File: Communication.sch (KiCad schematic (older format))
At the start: 24 parts, among them IC1 LAN8720

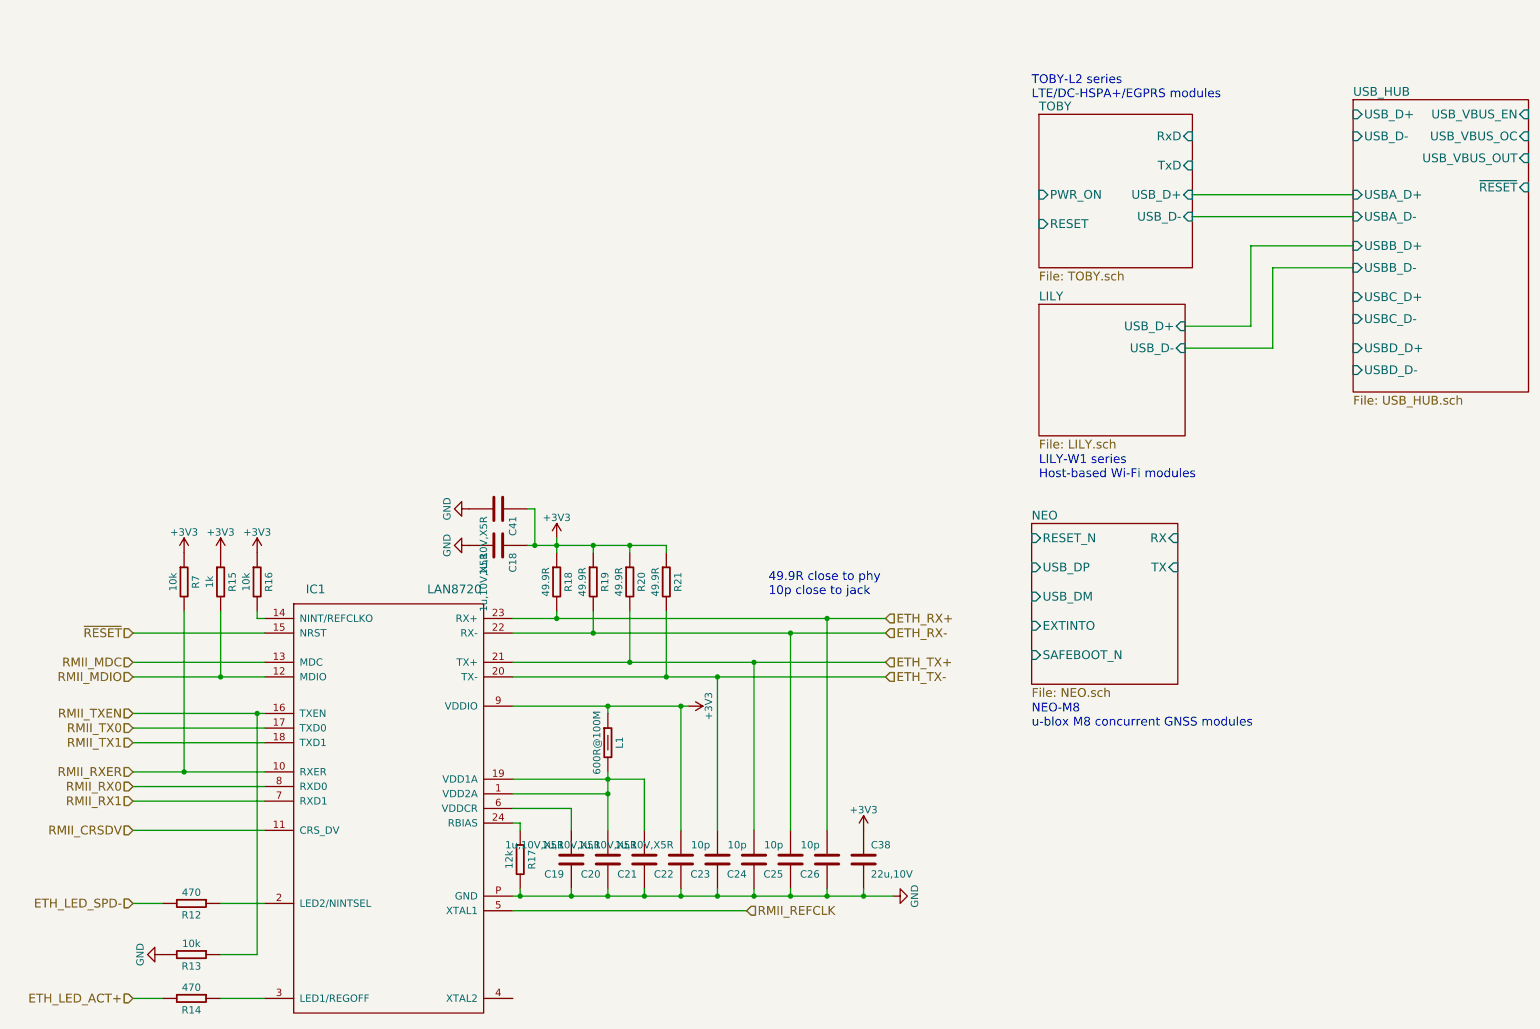
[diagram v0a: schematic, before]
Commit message: LAN Transformer footprint ergänzt
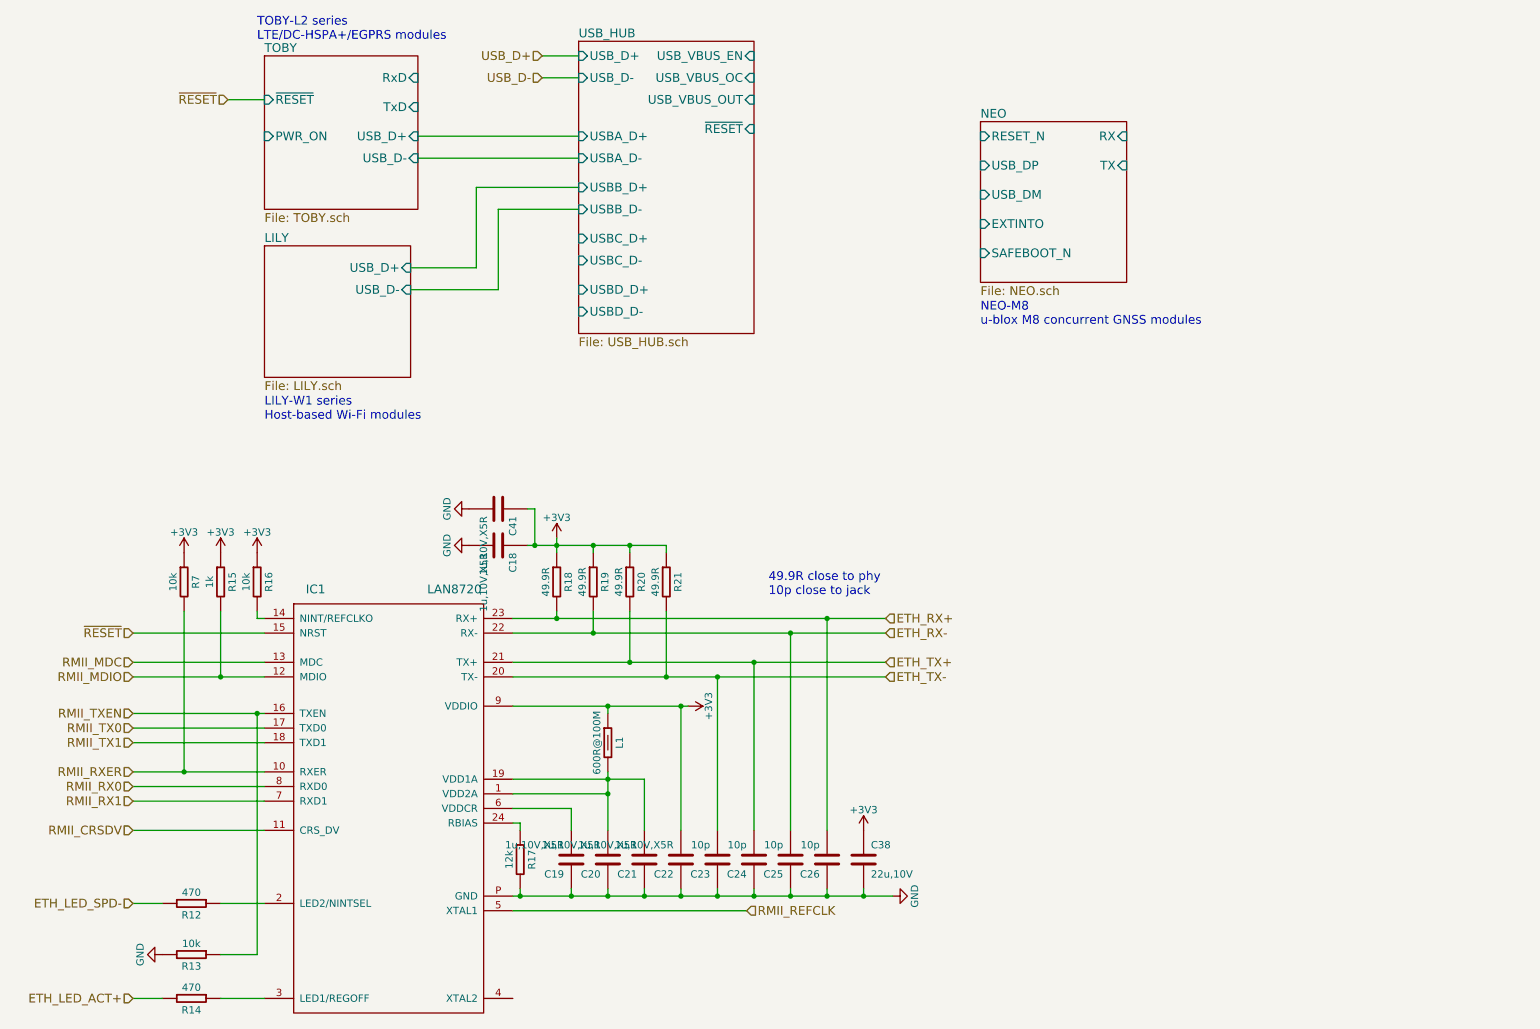
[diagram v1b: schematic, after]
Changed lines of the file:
@@
 	1400 6300 2300 6300
 $Sheet
-S 7600 1400 1050 1050
+S 2300 1000 1050 1050
 U 570DCCC5
 F0 "TOBY" 60
 F1 "TOBY.sch" 60
-F2 "PWR_ON" I L 7600 1950 60
-F3 "RESET" I L 7600 2150 60
-F4 "RxD" I R 8650 1550 60
-F5 "TxD" I R 8650 1750 60
-F6 "USB_D+" I R 8650 1950 60
-F7 "USB_D-" I R 8650 2100 60
+F2 "PWR_ON" I L 2300 1550 60
+F3 "RxD" I R 3350 1150 60
+F4 "TxD" I R 3350 1350 60
+F5 "USB_D+" I R 3350 1550 60
+F6 "USB_D-" I R 3350 1700 60
+F7 "~RESET" I L 2300 1300 60
 $EndSheet
-Text Notes 7550 1300 0    60   ~ 0
+Text Notes 2250 900  0    60   ~ 0
 TOBY-L2 series \nLTE/DC-HSPA+/EGPRS modules \n
 $Sheet
-S 7600 2700 1000 900
+S 2300 2300 1000 900
 U 57112592
 F0 "LILY" 60
 F1 "LILY.sch" 60
-F2 "USB_D+" I R 8600 2850 60
-F3 "USB_D-" I R 8600 3000 60
+F2 "USB_D+" I R 3300 2450 60
+F3 "USB_D-" I R 3300 2600 60
 $EndSheet
 $Sheet
-S 7550 4200 1000 1100
+S 7200 1450 1000 1100
 U 5712437A
 F0 "NEO" 60
 F1 "NEO.sch" 60
-F2 "RESET_N" I L 7550 4300 60
-F3 "USB_DP" I L 7550 4500 60
-F4 "USB_DM" I L 7550 4700 60
-F5 "EXTINTO" I L 7550 4900 60
-F6 "SAFEBOOT_N" I L 7550 5100 60
-F7 "RX" I R 8550 4300 60
-F8 "TX" I R 8550 4500 60
+F2 "RESET_N" I L 7200 1550 60
+F3 "USB_DP" I L 7200 1750 60
+F4 "USB_DM" I L 7200 1950 60
+F5 "EXTINTO" I L 7200 2150 60
+F6 "SAFEBOOT_N" I L 7200 2350 60
+F7 "RX" I R 8200 1550 60
+F8 "TX" I R 8200 1750 60
 $EndSheet
-Text Notes 7600 3900 0    60   ~ 0
+Text Notes 2300 3500 0    60   ~ 0
 LILY-W1 series \nHost-based Wi-Fi modules
-Text Notes 7550 5600 0    60   ~ 0
+Text Notes 7200 2850 0    60   ~ 0
 NEO-M8 \nu-blox M8 concurrent GNSS modules
 $Sheet
-S 9750 1300 1200 2000
+S 4450 900  1200 2000
 U 571531BA
 F0 "USB_HUB" 60
 F1 "USB_HUB.sch" 60
-F2 "USB_D+" I L 9750 1400 60
-F3 "USB_D-" I L 9750 1550 60
-F4 "USBA_D+" I L 9750 1950 60
-F5 "USBA_D-" I L 9750 2100 60
-F6 "USBB_D+" I L 9750 2300 60
-F7 "USBB_D-" I L 9750 2450 60
-F8 "USBC_D+" I L 9750 2650 60
-F9 "USBC_D-" I L 9750 2800 60
-F10 "USBD_D+" I L 9750 3000 60
-F11 "USBD_D-" I L 9750 3150 60
-F12 "~RESET" I R 10950 1900 60
-F13 "USB_VBUS_EN" I R 10950 1400 60
-F14 "USB_VBUS_OC" I R 10950 1550 60
-F15 "USB_VBUS_OUT" I R 10950 1700 60
+F2 "USB_D+" I L 4450 1000 60
+F3 "USB_D-" I L 4450 1150 60
+F4 "USBA_D+" I L 4450 1550 60
+F5 "USBA_D-" I L 4450 1700 60
+F6 "USBB_D+" I L 4450 1900 60
+F7 "USBB_D-" I L 4450 2050 60
+F8 "USBC_D+" I L 4450 2250 60
+F9 "USBC_D-" I L 4450 2400 60
+F10 "USBD_D+" I L 4450 2600 60
+F11 "USBD_D-" I L 4450 2750 60
+F12 "~RESET" I R 5650 1500 60
+F13 "USB_VBUS_EN" I R 5650 1000 60
+F14 "USB_VBUS_OC" I R 5650 1150 60
+F15 "USB_VBUS_OUT" I R 5650 1300 60
 $EndSheet
 Wire Wire Line
-	8650 1950 9750 1950
+	3350 1550 4450 1550
 Wire Wire Line
-	8650 2100 9750 2100
+	3350 1700 4450 1700
 Wire Wire Line
-	8600 2850 9050 2850
+	3300 2450 3750 2450
 Wire Wire Line
-	9050 2850 9050 2300
+	3750 2450 3750 1900
 Wire Wire Line
-	9050 2300 9750 2300
+	3750 1900 4450 1900
 Wire Wire Line
-	8600 3000 9200 3000
+	3300 2600 3900 2600
 Wire Wire Line
-	9750 2450 9200 2450
+	4450 2050 3900 2050
 Wire Wire Line
-	9200 2450 9200 3000
+	3900 2050 3900 2600
+Text HLabel 4200 1000 0    60   Input ~ 0
+USB_D+
+Text HLabel 4200 1150 0    60   Input ~ 0
+USB_D-
+Wire Wire Line
+	4200 1000 4450 1000
+Wire Wire Line
+	4200 1150 4450 1150
+Text HLabel 2050 1300 0    60   Input ~ 0
+~RESET
+Wire Wire Line
+	2050 1300 2300 1300
 $EndSCHEMATC

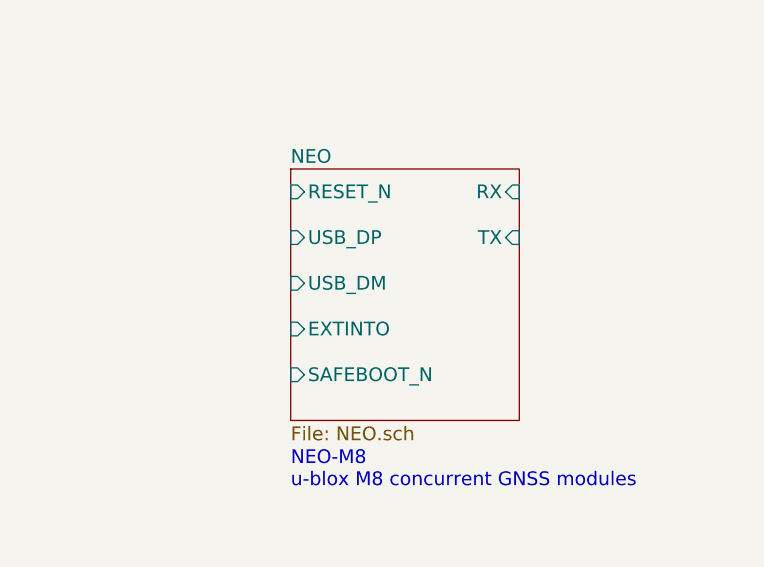
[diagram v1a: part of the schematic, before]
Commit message: NEO N8P durch M8N ersätzt
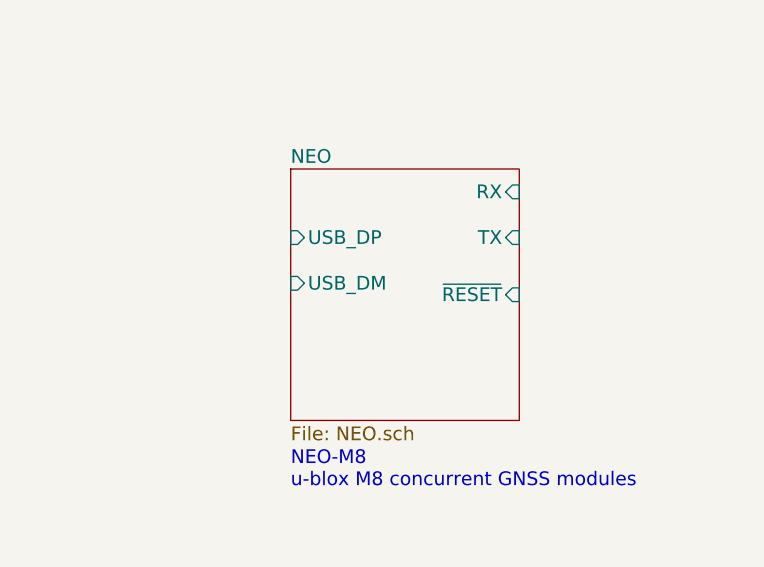
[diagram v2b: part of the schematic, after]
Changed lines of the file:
@@
 F3 "USB_D-" I R 3300 2600 60
-$EndSheet
-$Sheet
-S 7200 1450 1000 1100
-U 5712437A
-F0 "NEO" 60
-F1 "NEO.sch" 60
-F2 "RESET_N" I L 7200 1550 60
-F3 "USB_DP" I L 7200 1750 60
-F4 "USB_DM" I L 7200 1950 60
-F5 "EXTINTO" I L 7200 2150 60
-F6 "SAFEBOOT_N" I L 7200 2350 60
-F7 "RX" I R 8200 1550 60
-F8 "TX" I R 8200 1750 60
 $EndSheet
 Text Notes 2300 3500 0    60   ~ 0
@@
 Wire Wire Line
 	2050 1300 2300 1300
+$Sheet
+S 7200 1450 1000 1100
+U 5712437A
+F0 "NEO" 60
+F1 "NEO.sch" 60
+F2 "USB_DP" I L 7200 1750 60
+F3 "USB_DM" I L 7200 1950 60
+F4 "RX" I R 8200 1550 60
+F5 "TX" I R 8200 1750 60
+F6 "~RESET" I R 8200 2000 60
+$EndSheet
 $EndSCHEMATC

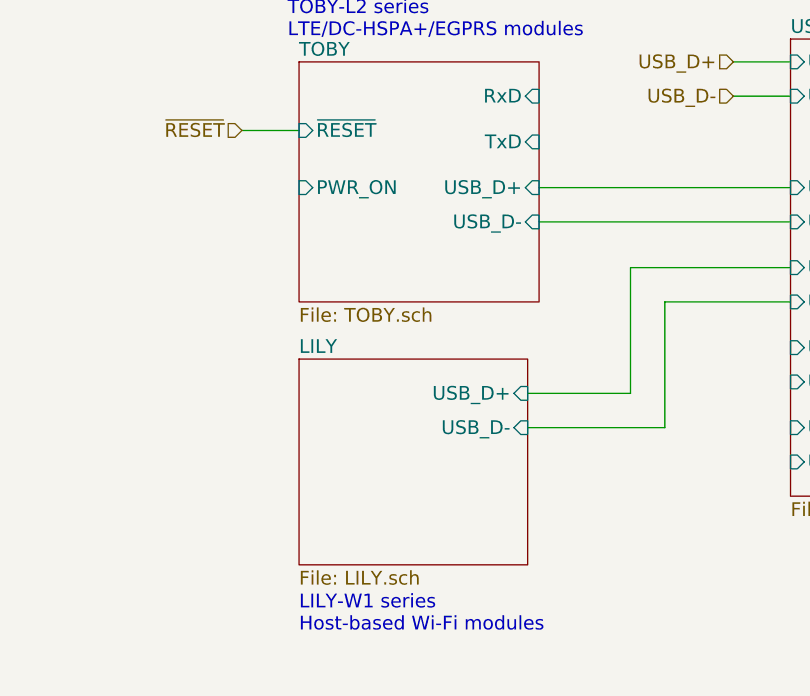
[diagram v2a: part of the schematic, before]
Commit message: footprints ergänzt
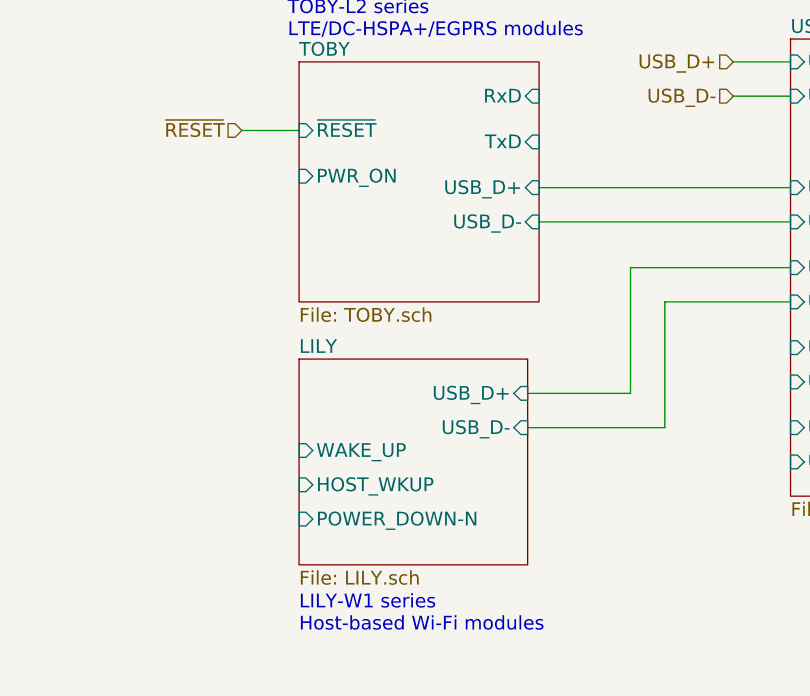
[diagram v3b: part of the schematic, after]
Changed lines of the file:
@@
 F0 "TOBY" 60
 F1 "TOBY.sch" 60
-F2 "PWR_ON" I L 2300 1550 60
-F3 "RxD" I R 3350 1150 60
-F4 "TxD" I R 3350 1350 60
-F5 "USB_D+" I R 3350 1550 60
-F6 "USB_D-" I R 3350 1700 60
-F7 "~RESET" I L 2300 1300 60
+F2 "RxD" I R 3350 1150 60
+F3 "TxD" I R 3350 1350 60
+F4 "USB_D+" I R 3350 1550 60
+F5 "USB_D-" I R 3350 1700 60
+F6 "~RESET" I L 2300 1300 60
+F7 "PWR_ON" I L 2300 1500 60
 $EndSheet
 Text Notes 2250 900  0    60   ~ 0
@@
 F2 "USB_D+" I R 3300 2450 60
 F3 "USB_D-" I R 3300 2600 60
+F4 "WAKE_UP" I L 2300 2700 60
+F5 "HOST_WKUP" I L 2300 2850 60
+F6 "POWER_DOWN-N" I L 2300 3000 60
 $EndSheet
 Text Notes 2300 3500 0    60   ~ 0
